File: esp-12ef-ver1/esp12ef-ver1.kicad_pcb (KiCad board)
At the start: 2 copper layers, 92.7 x 40.6 mm, 18 parts, among them J1 Battery, J2 USB-TTL, J3 BME280_CONNECTOR, SW1 RESET, U1 ESP-12F

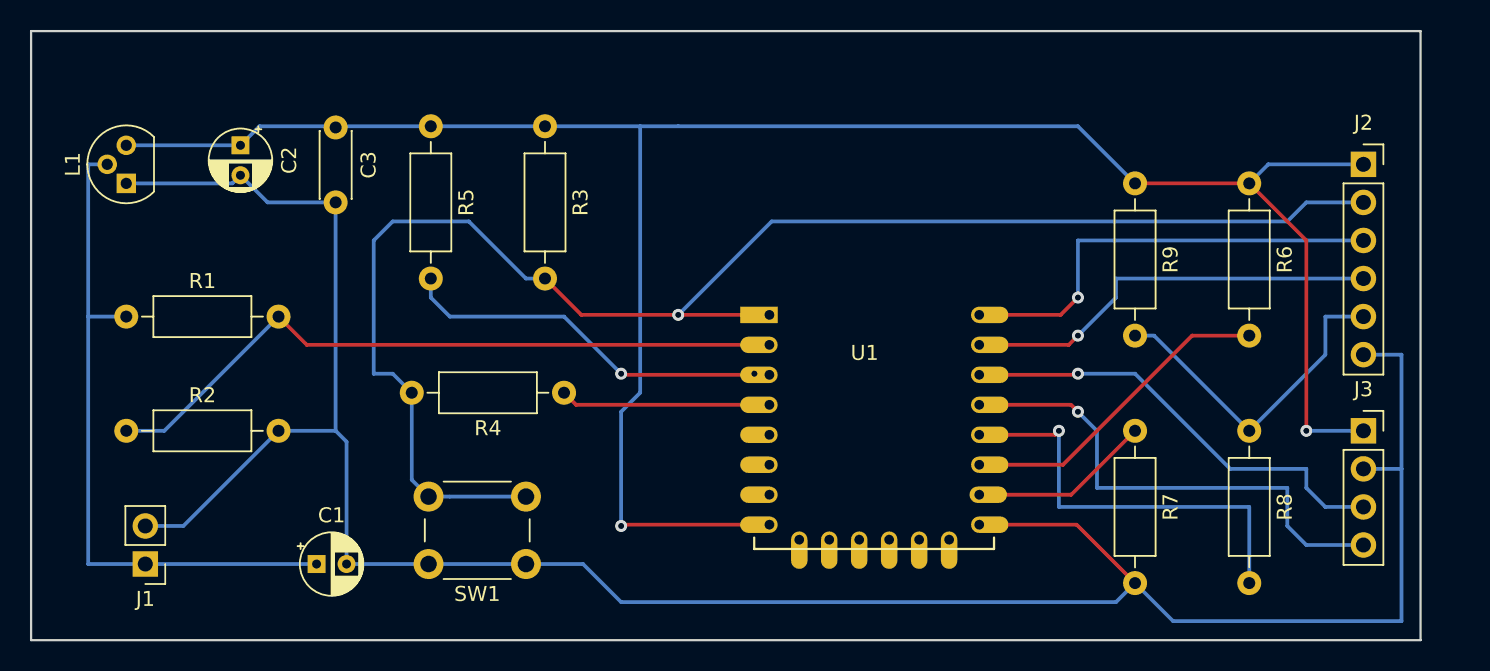
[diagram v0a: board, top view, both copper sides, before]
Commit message: уменьшен размер платы
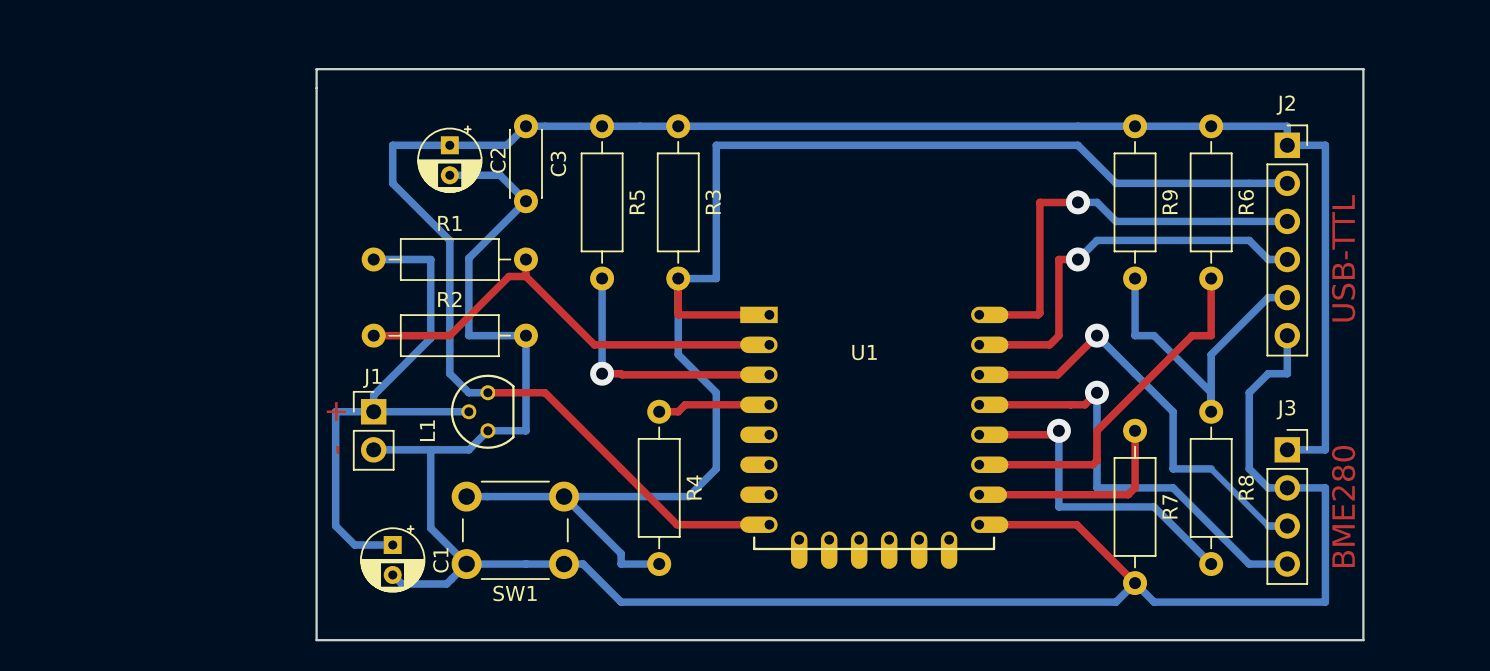
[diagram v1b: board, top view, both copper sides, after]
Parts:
- L1: footprint Package_TO_SOT_THT:TO-92 -> ht7333-a:ht7333-a
- moved L1 29.2 mm to (106.7, 90.2)
- moved J1 18.3 mm to (99.1, 88.9), turned to 0 degrees
- moved R2 17.7 mm to (99.1, 83.8)
- moved R1 16.9 mm to (99.1, 78.7)
- moved C2 14.0 mm to (104.1, 71.1)
- moved C3 12.7 mm to (109.2, 69.8)
- moved R5 11.4 mm to (114.3, 69.8)
- moved R3 8.89 mm to (119.4, 69.8)
- moved R4 6.48 mm to (118.1, 88.9), turned to 270 degrees
- moved C1 5.24 mm to (100.3, 97.8), turned to 270 degrees
- moved J2 5.24 mm to (160.0, 71.1)
- moved J3 5.24 mm to (160.0, 91.4)
- moved R6 4.58 mm to (154.9, 69.8)
- moved R9 3.81 mm to (149.9, 69.8)
- moved R8 2.84 mm to (154.9, 88.9)
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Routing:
- net Net-(R1-Pad2): track 46.9 -> 31.1 mm
- net Net-(C1-Pad2): track 162.8 -> 147.1 mm
- net Net-(C2-Pad1): track 144.2 -> 129.2 mm, vias 2 -> 0
- net Net-(C1-Pad1): track 45.7 -> 36.4 mm
- net Net-(R5-Pad2): track 26.0 -> 17.5 mm, vias 2 -> 1
- net Net-(R4-Pad1): track 14.0 -> 7.55 mm
- net Net-(R8-Pad2): track 28.3 -> 22.2 mm
- net Net-(J2-Pad2): track 104.2 -> 100.2 mm, vias 1 -> 0
- net SDA: track 33.2 -> 29.3 mm
- net Net-(R6-Pad2): track 21.6 -> 24.0 mm
- net Net-(R7-Pad1): track 12.5 -> 14.7 mm
- net Net-(J2-Pad3): track 29.9 -> 28.5 mm
- net Net-(J2-Pad4): track 28.2 -> 26.9 mm
- net Net-(J2-Pad5): track 22.5 -> 21.5 mm
- net SCL: track 30.1 -> 29.1 mm
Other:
- board size 92.7 x 40.6 mm -> 69.8 x 38.1 mm
- net class Default: clearance 0.25 -> 0.5; trace_width 0.25 -> 0.5; via_dia 0.8 -> 1.6; via_drill 0.4 -> 0.8
- rule trace_clearance: 0.25 -> 0.5
- board text added: "+"
- board text added: "-"
- board text added: "BME280"
- board text added: "USB-TTL"

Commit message: пытаемся развести smd в один слой
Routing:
- net (no net): vias 0 -> 4
- added copper zone on B.Cu, net Net-(C1-Pad2)
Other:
- board size 69.8 x 38.1 mm -> 82.5 x 38.1 mm
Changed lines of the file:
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@@
   (general
     (thickness 1.6)
-    (drawings 9)
-    (tracks 157)
+    (drawings 13)
+    (tracks 161)
     (zones 0)
     (modules 18)
@@
     (last_trace_width 0.5)
     (trace_clearance 0.5)
-    (zone_clearance 0.508)
+    (zone_clearance 0.5)
     (zone_45_only no)
     (trace_min 0.25)
@@
     )
   )
+  (gr_line (start 171.45 104.14) (end 165.1 104.14) (layer Edge.Cuts) (width 0.15))
+  (gr_line (start 171.45 66.04) (end 171.45 104.14) (layer Edge.Cuts) (width 0.15))
+  (gr_line (start 165.1 66.04) (end 171.45 66.04) (layer Edge.Cuts) (width 0.15))
+  (gr_line (start 88.9 104.14) (end 95.25 104.14) (layer Edge.Cuts) (width 0.15))
+  (gr_line (start 88.9 66.04) (end 88.9 67.31) (layer Edge.Cuts) (width 0.15))
+  (gr_line (start 95.25 66.04) (end 88.9 66.04) (layer Edge.Cuts) (width 0.15))
   (gr_text - (at 96.52 91.44 90) (layer F.Cu)
     (effects (font (size 1.5 1.5) (thickness 0.3)))
@@
     (effects (font (size 1.5 1.5) (thickness 0.3)))
   )
-  (gr_line (start 95.25 66.04) (end 95.25 67.31) (layer Edge.Cuts) (width 0.15))
   (gr_line (start 165.1 66.04) (end 95.25 66.04) (layer Edge.Cuts) (width 0.15))
-  (gr_line (start 165.1 104.14) (end 165.1 66.04) (layer Edge.Cuts) (width 0.15))
   (gr_line (start 95.25 104.14) (end 165.1 104.14) (layer Edge.Cuts) (width 0.15))
-  (gr_line (start 95.25 67.31) (end 95.25 104.14) (layer Edge.Cuts) (width 0.15))
+  (gr_line (start 88.9 67.31) (end 88.9 104.14) (layer Edge.Cuts) (width 0.15))
+  (via (at 93.98 71.12) (size 3) (drill 0.2) (layers F.Cu B.Cu) (net 0))
+  (via (at 93.98 100.33) (size 3) (drill 0.2) (layers F.Cu B.Cu) (net 0))
+  (via (at 167.64 100.33) (size 3) (drill 0.2) (layers F.Cu B.Cu) (net 0))
+  (via (at 167.64 71.12) (size 3) (drill 0.2) (layers F.Cu B.Cu) (net 0))
   (segment (start 139.465001 96.435001) (end 139.625002 96.275) (width 0.5) (layer F.Cu) (net 1))
   (segment (start 139.465001 96.435001) (end 145.965001 96.435001) (width 0.5) (layer F.Cu) (net 1))
@@
   (segment (start 125.465001 96.435001) (end 119.295001 96.435001) (width 0.5) (layer F.Cu) (net 3))
   (segment (start 119.295001 96.435001) (end 115.57 92.71) (width 0.5) (layer F.Cu) (net 3))
-  (segment (start 160.02 73.66) (end 158.75 73.66) (width 0.5) (layer B.Cu) (net 4))
   (segment (start 154.94 69.85) (end 149.86 69.85) (width 0.5) (layer B.Cu) (net 3))
   (segment (start 149.86 69.85) (end 146.05 69.85) (width 0.5) (layer B.Cu) (net 3))
@@
   (segment (start 160.02 71.12) (end 160.02 69.85) (width 0.5) (layer B.Cu) (net 3))
   (segment (start 160.02 69.85) (end 154.94 69.85) (width 0.5) (layer B.Cu) (net 3))
+  (segment (start 160.02 73.66) (end 158.75 73.66) (width 0.5) (layer B.Cu) (net 4))
   (segment (start 125.465001 82.435001) (end 119.38 82.435001) (width 0.5) (layer F.Cu) (net 4))
   (segment (start 119.38 82.435001) (end 119.38 80.01) (width 0.5) (layer F.Cu) (net 4))
@@
   (segment (start 154.94 99.06) (end 151.13 95.25) (width 0.5) (layer B.Cu) (net 15))
   (segment (start 151.13 95.25) (end 144.78 95.25) (width 0.5) (layer B.Cu) (net 15))
+  (zone (net 1) (net_name "Net-(C1-Pad2)") (layer B.Cu) (hatch edge 0.508)
+    (connect_pads (clearance 0.5))
+    (min_thickness 0.254)
+    (fill yes (arc_segments 16) (thermal_gap 0.508) (thermal_bridge_width 0.508) (smoothing fillet))
+    (polygon
+      (pts
+        (xy 88.9 66.04) (xy 88.9 104.14) (xy 171.45 104.14) (xy 171.45 66.04)
+      )
+    )
+  )
+  (zone (net 0) (net_name "") (layer B.Cu) (hatch edge 0.508)
+    (connect_pads (clearance 0.5))
+    (min_thickness 0.254)
+    (keepout (tracks not_allowed) (vias not_allowed) (copperpour not_allowed))
+    (fill (arc_segments 16) (thermal_gap 0.508) (thermal_bridge_width 0.508))
+    (polygon
+      (pts
+        (xy 123.19 72.39) (xy 123.19 81.28) (xy 142.24 81.28) (xy 142.24 72.39)
+      )
+    )
+  )
 )
